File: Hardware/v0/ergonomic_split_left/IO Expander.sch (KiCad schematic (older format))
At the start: 4 parts, among them U2 PCAL9555AHF

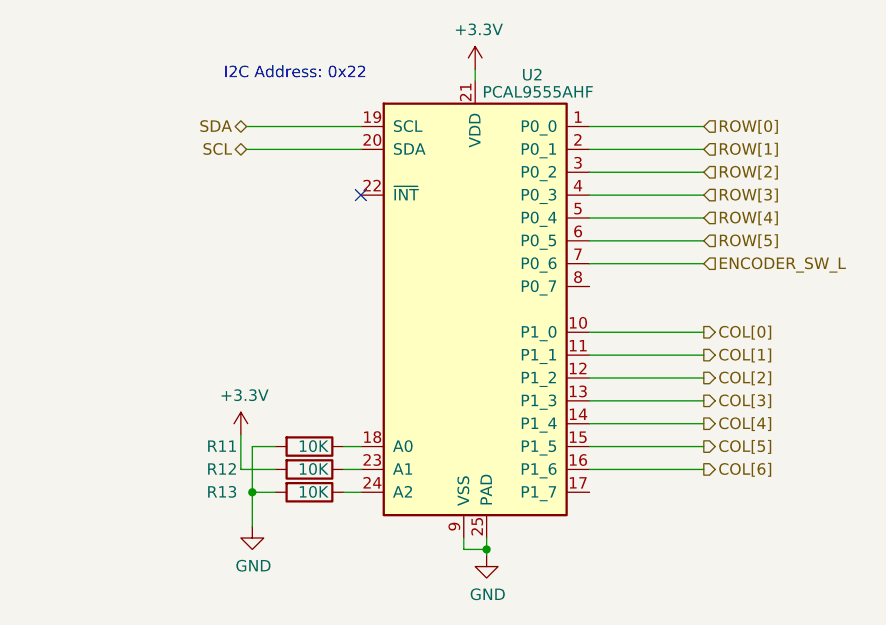
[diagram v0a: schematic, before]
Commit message: Drawing board outline Basic placement done Adding rotary encoder to the switch matrix Adding mounting holes
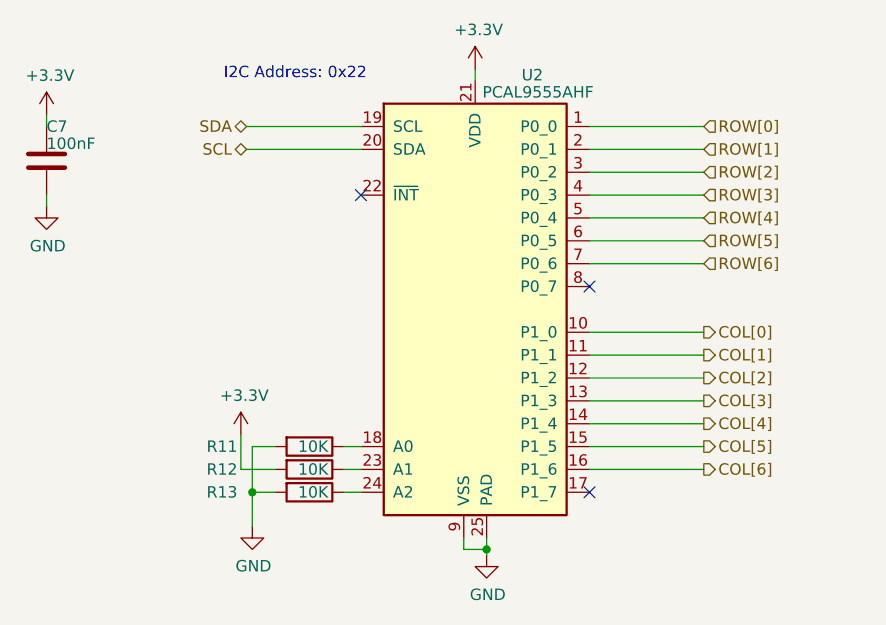
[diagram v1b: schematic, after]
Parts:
- added C7: 100nF, Capacitor_smd:C_0603_1608Metric, symbol Device:C
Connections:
- net +3V3: now also C7.1
- net GND: now also C7.2
- net ENCODER_SW_L renamed ROW[6]
- no-connect marks 1 -> 3
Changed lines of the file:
@@
 	4625 4325 4775 4325
 Text HLabel 6650 3425 2    50   Input ~ 0
-ENCODER_SW_L
+ROW[6]
 Wire Wire Line
 	6650 3425 6150 3425
+Wire Wire Line
+	3775 2825 3775 2775
+Wire Wire Line
+	3775 3125 3775 3175
+$Comp
+L power:GND #PWR?
+U 1 1 62EDB2E6
+P 3775 3175
+AR Path="/62EDB2E6" Ref="#PWR?"  Part="1"
+AR Path="/60D44BDB/62EDB2E6" Ref="#PWR?"  Part="1"
+AR Path="/62022D96/62EDB2E6" Ref="#PWR?"  Part="1"
+AR Path="/612342D1/62EDB2E6" Ref="#PWR?"  Part="1"
+AR Path="/63013830/62EDB2E6" Ref="#PWR?"  Part="1"
+AR Path="/62999575/62EDB2E6" Ref="#PWR?"  Part="1"
+AR Path="/629997F8/62EDB2E6" Ref="#PWR017"  Part="1"
+F 0 "#PWR017" H 3775 2925 50  0001 C CNN
+F 1 "GND" H 3780 3002 50  0000 C CNN
+F 2 "" H 3775 3175 50  0001 C CNN
+F 3 "" H 3775 3175 50  0001 C CNN
+	1    3775 3175
+	1    0    0    -1
+$EndComp
+$Comp
+L Device:C C?
+U 1 1 62EDB2EC
+P 3775 2975
+AR Path="/62EDB2EC" Ref="C?"  Part="1"
+AR Path="/60D44BDB/62EDB2EC" Ref="C?"  Part="1"
+AR Path="/62022D96/62EDB2EC" Ref="C?"  Part="1"
+AR Path="/612342D1/62EDB2EC" Ref="C?"  Part="1"
+AR Path="/63013830/62EDB2EC" Ref="C?"  Part="1"
+AR Path="/62999575/62EDB2EC" Ref="C?"  Part="1"
+AR Path="/629997F8/62EDB2EC" Ref="C7"  Part="1"
+F 0 "C7" H 3775 3125 50  0000 L CNN
+F 1 "100nF" H 3775 3050 50  0000 L CNN
+F 2 "Capacitor_smd:C_0603_1608Metric" H 3813 2825 50  0001 C CNN
+F 3 "~" H 3775 2975 50  0001 C CNN
+	1    3775 2975
+	1    0    0    -1
+$EndComp
+$Comp
+L power:+3.3V #PWR?
+U 1 1 62EDB2F2
+P 3775 2775
+AR Path="/62EDB2F2" Ref="#PWR?"  Part="1"
+AR Path="/60D44BDB/62EDB2F2" Ref="#PWR?"  Part="1"
+AR Path="/62022D96/62EDB2F2" Ref="#PWR?"  Part="1"
+AR Path="/612342D1/62EDB2F2" Ref="#PWR?"  Part="1"
+AR Path="/63013830/62EDB2F2" Ref="#PWR?"  Part="1"
+AR Path="/62999575/62EDB2F2" Ref="#PWR?"  Part="1"
+AR Path="/629997F8/62EDB2F2" Ref="#PWR016"  Part="1"
+F 0 "#PWR016" H 3775 2625 50  0001 C CNN
+F 1 "+3.3V" H 3790 2948 50  0000 C CNN
+F 2 "" H 3775 2775 50  0001 C CNN
+F 3 "" H 3775 2775 50  0001 C CNN
+	1    3775 2775
+	1    0    0    -1
+$EndComp
+NoConn ~ 6150 3525
+NoConn ~ 6150 4425
 $EndSCHEMATC

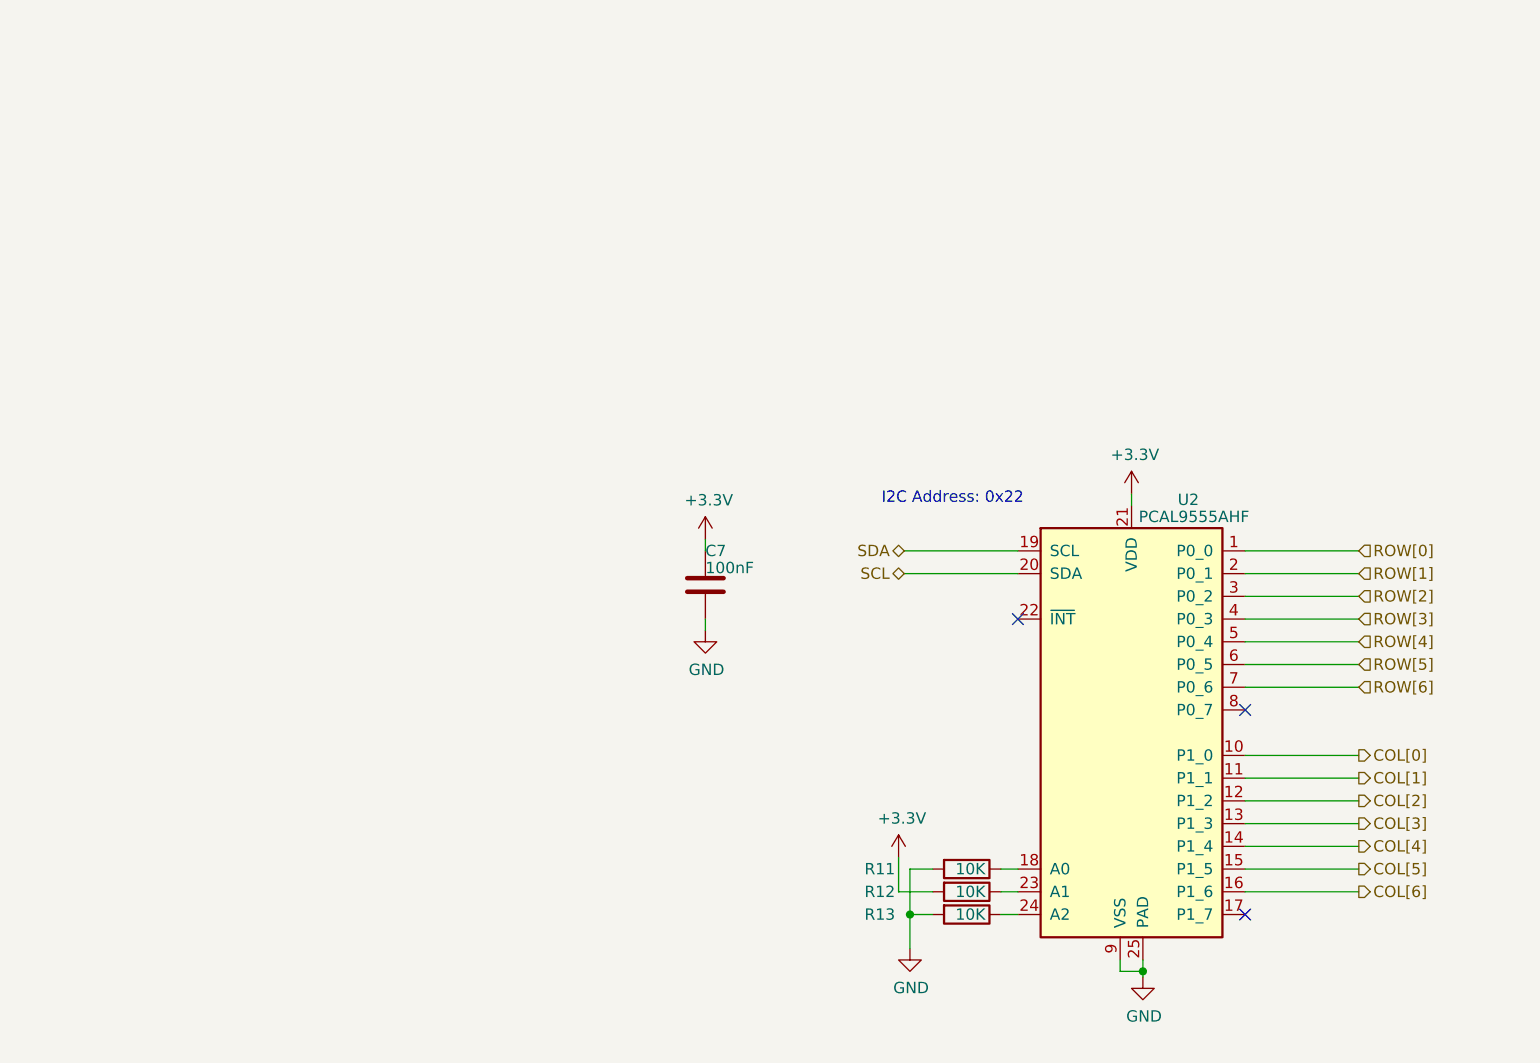
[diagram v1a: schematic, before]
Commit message: Debug connectors Adding I2C debug header Changed SPI programming header to edge mount Changed right interface connector to IDC Cleaning up schematic
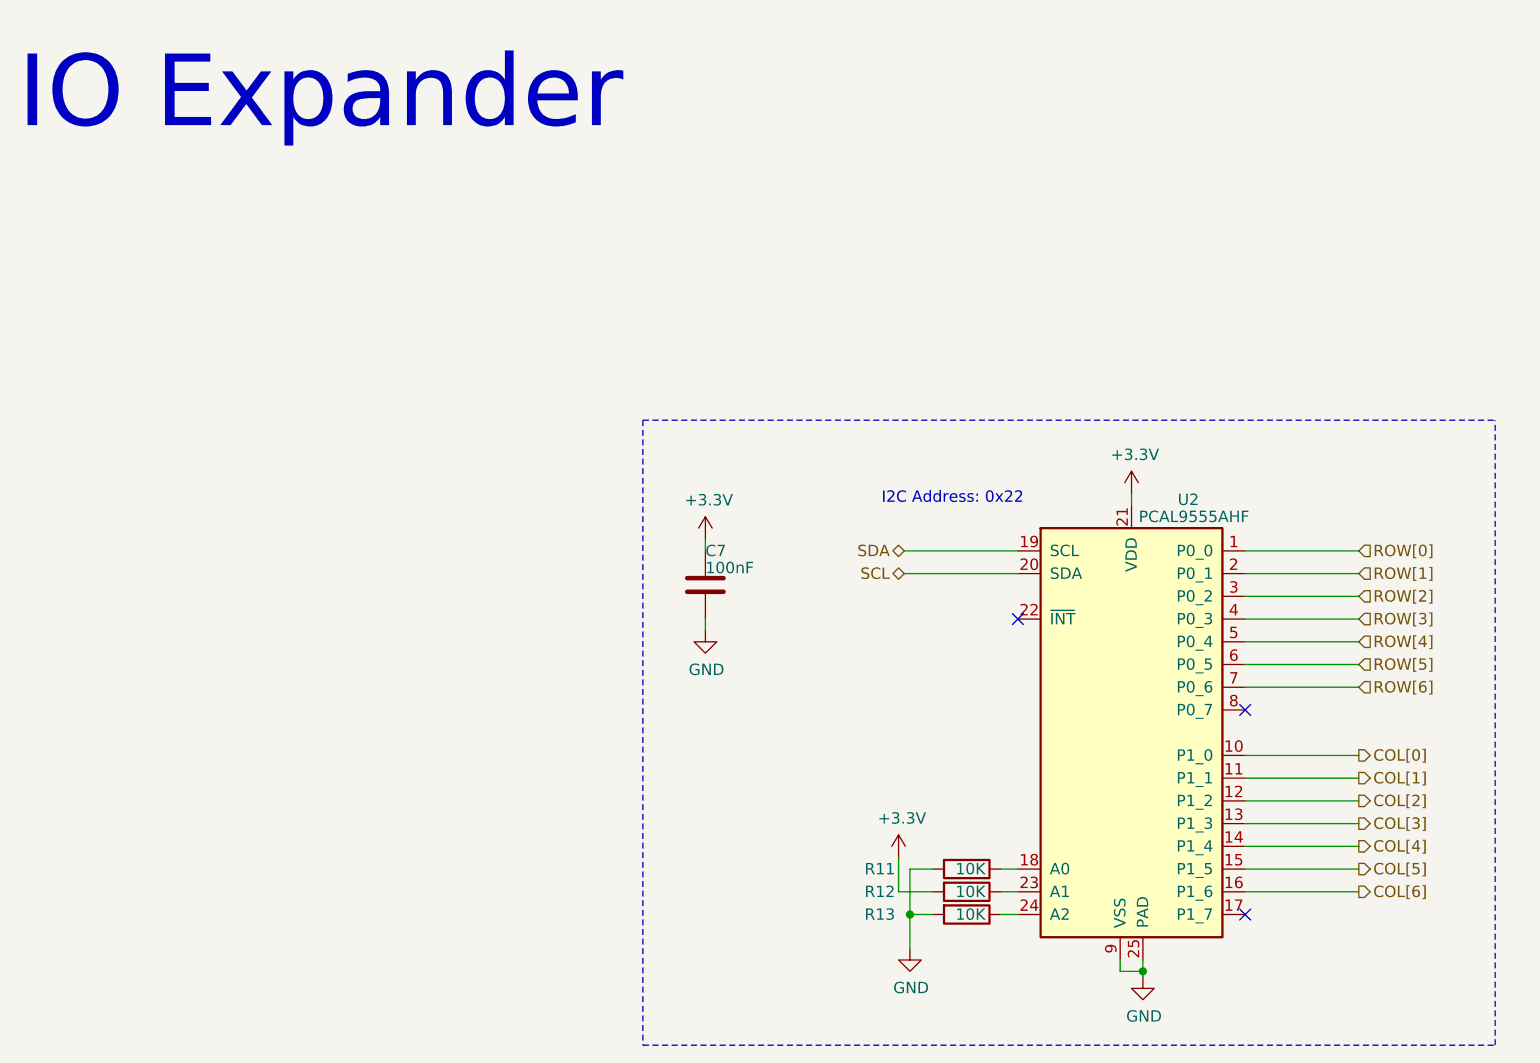
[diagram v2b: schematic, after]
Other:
- note added: "IO Expander"
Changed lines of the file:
@@
 NoConn ~ 6150 3525
 NoConn ~ 6150 4425
+Text Notes 750  1000 0    315  ~ 0
+IO Expander
+Wire Notes Line
+	3500 5000 7250 5000
+Wire Notes Line
+	3500 2250 3500 5000
+Wire Notes Line
+	7250 5000 7250 2250
+Wire Notes Line
+	3500 2250 7250 2250
 $EndSCHEMATC
